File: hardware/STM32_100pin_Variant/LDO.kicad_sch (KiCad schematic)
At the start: 4 parts, among them U3 NCV8163

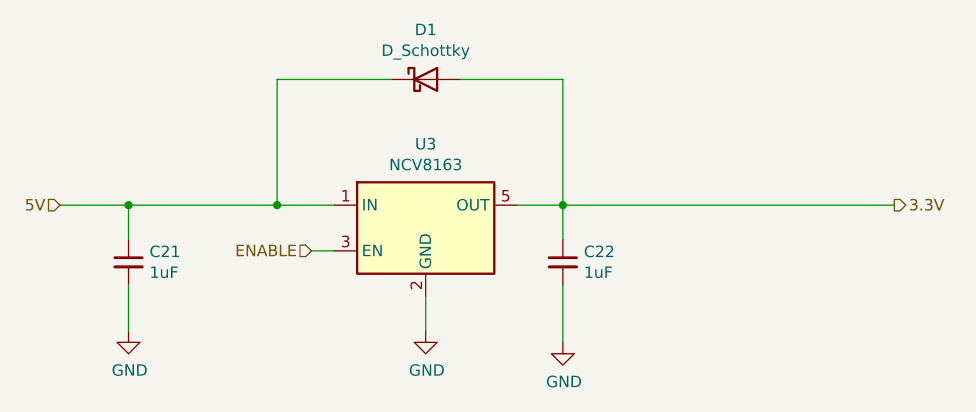
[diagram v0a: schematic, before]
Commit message: Schematic wiring fix, added part numbers
- Fixed missing connections between VREF+ and VDDA, VREF- and VSSA on all ECUs

- Added component part numbers for crystal and CAN trx to schematic
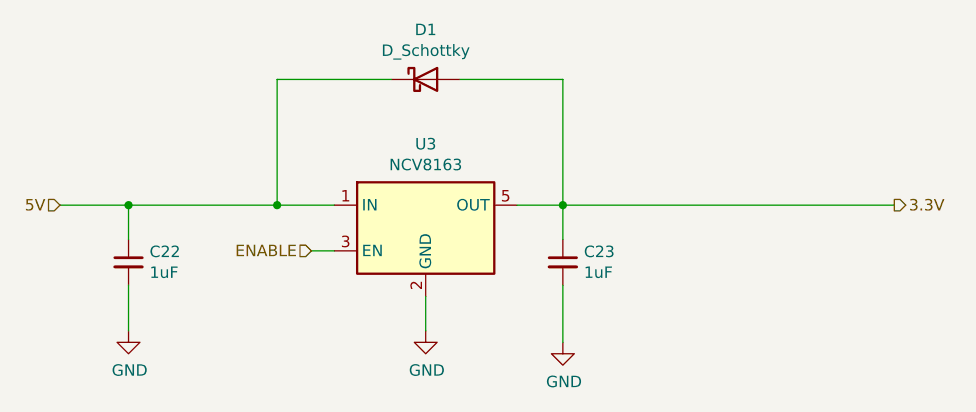
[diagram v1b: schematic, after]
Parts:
- renumbered C21 to C22, C22 to C23
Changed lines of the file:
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@@
   (symbol (lib_id "Device:C_Small") (at 81.28 77.47 0) (unit 1)
     (in_bom yes) (on_board yes)
-    (property "Reference" "C21" (id 0) (at 83.6168 76.3016 0)
+    (property "Reference" "C22" (id 0) (at 83.6168 76.3016 0)
       (effects (font (size 1.27 1.27)) (justify left))
     )
@@
   (symbol (lib_id "Device:C_Small") (at 129.54 77.47 0) (unit 1)
     (in_bom yes) (on_board yes)
-    (property "Reference" "C22" (id 0) (at 131.8768 76.3016 0)
+    (property "Reference" "C23" (id 0) (at 131.8768 76.3016 0)
       (effects (font (size 1.27 1.27)) (justify left))
     )
@@
   (symbol (lib_id "power:GND") (at 114.3 85.09 0) (unit 1)
     (in_bom yes) (on_board yes)
-    (property "Reference" "#PWR031" (id 0) (at 114.3 91.44 0)
+    (property "Reference" "#PWR032" (id 0) (at 114.3 91.44 0)
       (effects (font (size 1.27 1.27)) hide)
     )
@@
   (symbol (lib_id "power:GND") (at 129.54 86.36 0) (unit 1)
     (in_bom yes) (on_board yes)
-    (property "Reference" "#PWR032" (id 0) (at 129.54 92.71 0)
+    (property "Reference" "#PWR033" (id 0) (at 129.54 92.71 0)
       (effects (font (size 1.27 1.27)) hide)
     )
@@
   (symbol (lib_id "power:GND") (at 81.28 85.09 0) (unit 1)
     (in_bom yes) (on_board yes)
-    (property "Reference" "#PWR030" (id 0) (at 81.28 91.44 0)
+    (property "Reference" "#PWR031" (id 0) (at 81.28 91.44 0)
       (effects (font (size 1.27 1.27)) hide)
     )

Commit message: Electrical Fix
- Fixed missing VREF+/- connections on ECUs

- Updated version number to V1.1

- Updated Gerbers

- Updated schematic PDF
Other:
- title: RAMN: Resistant Automotive Miniature Network V1.0 -> RAMN 100 Pin Variant
